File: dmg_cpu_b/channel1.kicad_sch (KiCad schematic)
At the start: 123 parts

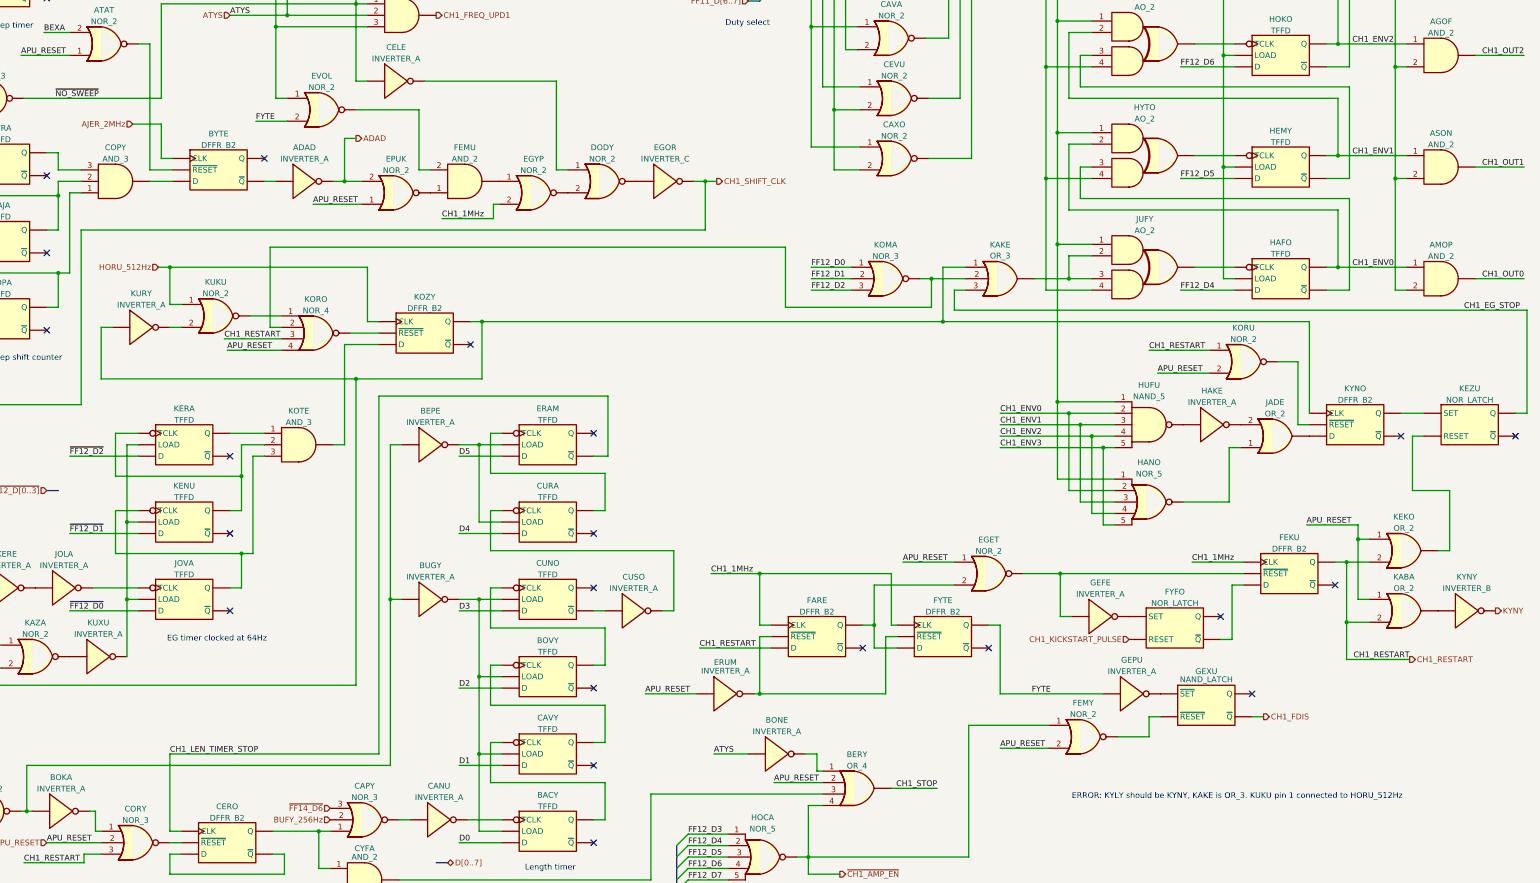
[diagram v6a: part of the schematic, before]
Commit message: Some mistakes found in APU sheets, notes added for clarity. Edit in PPU sheets following review.
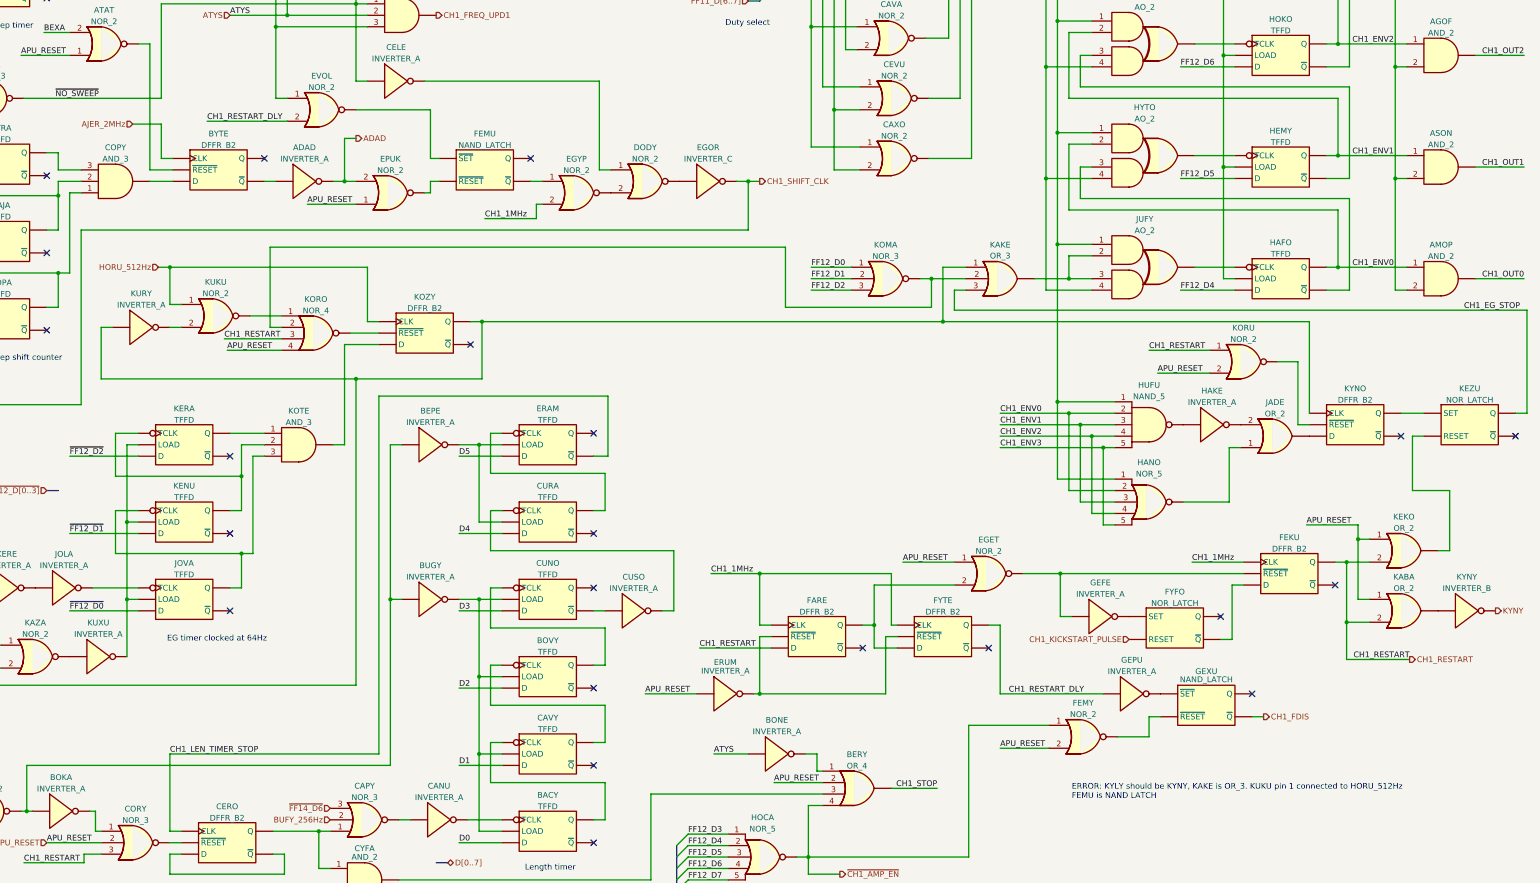
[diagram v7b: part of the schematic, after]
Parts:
- FEMU: value AND_2 -> NAND_LATCH; symbol DMG_CPU_Cells:AND_2 -> DMG_CPU_Cells:NAND_LATCH
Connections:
- net at FEMU.2 (~{Q}): now also EGYP.1; no longer EVOL.3
- net at FEMU.3 (Q): no longer EGYP.1
- net FYTE renamed CH1_RESTART_DLY
- new net: EVOL.3, FEMU.4 (~{SET})
- no-connect marks 28 -> 29
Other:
- note added: "ERROR: KYLY should be KYNY, KAKE is OR_3. KUKU pin 1 connected to HORU_512Hz FEMU is NAND LATCH"
- note removed: "ERROR: KYLY should be KYNY, KAKE is OR_3. KUKU pin 1 connected to HORU_512Hz"
- moved on the sheet: DODY, EGOR, EGYP, EPUK

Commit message: VRAM interface sheet added but various edits in existing sheets. Notable merge of RESET, CLOCKS and FF04 DIV sheets
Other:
- company: (none) -> CC-BY-SA-4.0 Régis Galland & Michael Singer -- Derived work from Furrtek
- title: (none) -> DMG CPU B
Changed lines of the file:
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@@
 (kicad_sch (version 20211123) (generator eeschema)
   (paper "A3")
+  (title_block
+    (title "DMG CPU B")
+    (date "2022-05-02")
+    (rev "0")
+    (company "CC-BY-SA-4.0 Régis Galland & Michael Singer -- Derived work from Furrtek")
+    (comment 1 "https://github.com/msinger/dmg-schematics")
+  )
   (junction (at 205.105 66.04) (diameter 0) (color 0 0 0 0)
   )
